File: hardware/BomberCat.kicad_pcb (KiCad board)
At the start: 2 copper layers, 65 x 84.8 mm, 111 parts, among them J1 Battery, J3 MAGSPOOF, J4 MAGSPOOF, P1 USB_C_Plug_USB2.0, Q1 DMG3415U-7, SW1 RESET, SW2 GPIO, SW3 ON, SW4 SOURCE MAG, U1 PN7150B0HN_C11006Y-PN7150B0HN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

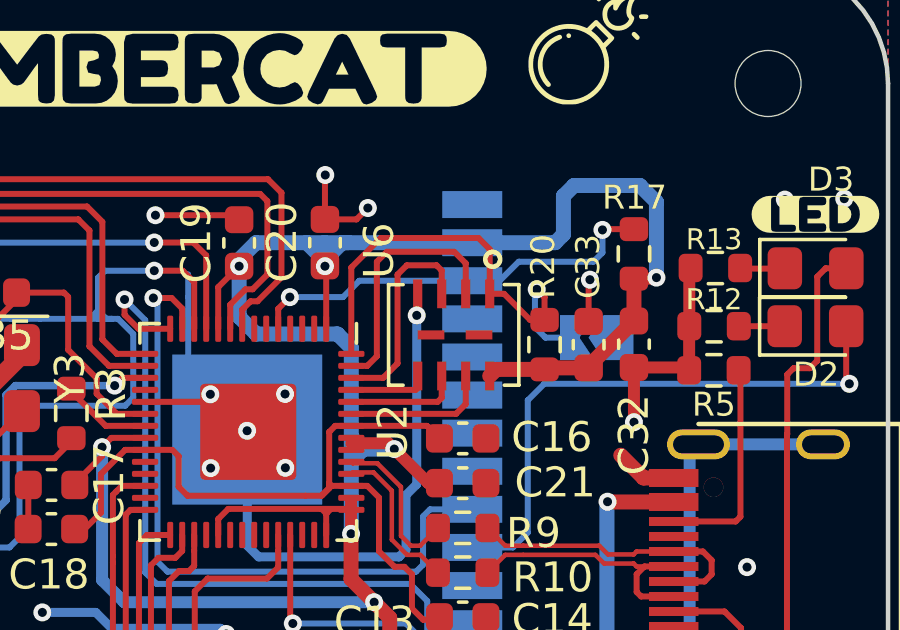
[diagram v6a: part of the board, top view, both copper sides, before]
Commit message: fix(Hw):No_part_Flash_Memory_Changed
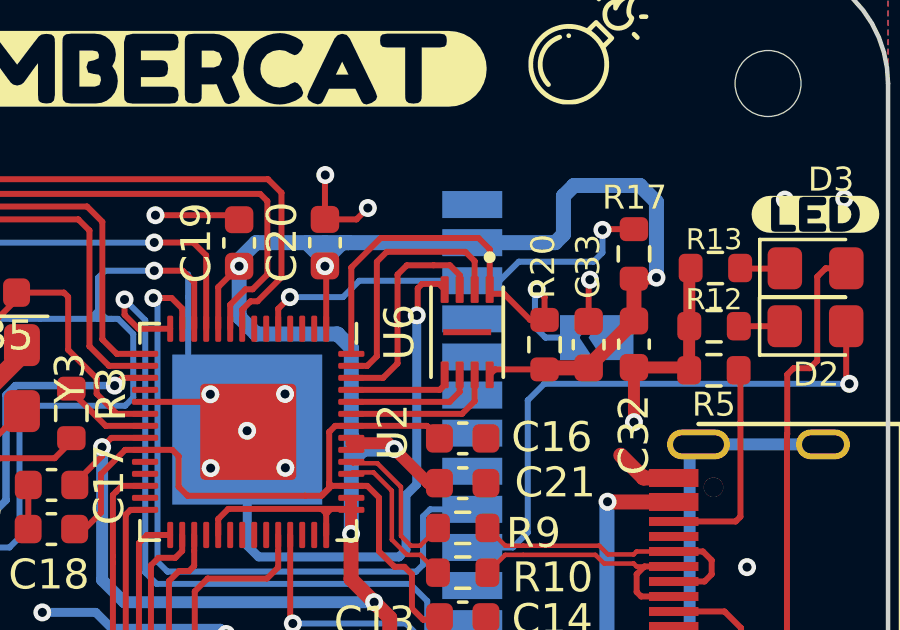
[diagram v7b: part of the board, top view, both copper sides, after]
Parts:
- U6: footprint BomberCat:W25Q16JVUUIQ -> BomberCat:SON50P200X300X40-9N
- moved U6 0.46 mm to (143.0, 148.3)
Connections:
- C35 pad 1: Net-(U2-GPIO14) -> Net-(U2-XIN)
- R3 pad 2: Net-(U2-GPIO16) -> Net-(U2-XOUT)
- U2 pad 10: unconnected-(U2-IOVDD-Pad10) -> +3V3
- U2 pad 11: unconnected-(U2-GPIO8-Pad11) -> /CIPO_TX
- U2 pad 12: unconnected-(U2-GPIO9-Pad12) -> /CS_RX
- U2 pad 13: unconnected-(U2-GPIO10-Pad13) -> /ACK_CTS
- U2 pad 14: unconnected-(U2-GPIO11-Pad14) -> /COPI_RTS
- U2 pad 15: unconnected-(U2-GPIO12-Pad15) -> /SDA
- U2 pad 16: unconnected-(U2-GPIO13-Pad16) -> /SCL
- U2 pad 17: Net-(U2-GPIO14) -> /SCK
- U2 pad 19: unconnected-(U2-TESTEN-Pad19) -> GND
- U2 pad 20: /SCK -> Net-(U2-XIN)
- U2 pad 21: unconnected-(U2-XOUT-Pad21) -> Net-(U2-XOUT)
- U2 pad 23: unconnected-(U2-DVDD-Pad23) -> +1V2
- U2 pad 24: unconnected-(U2-SWCLK-Pad24) -> /SWCLK
- U2 pad 25: unconnected-(U2-SWD-Pad25) -> /SWDIO
- U2 pad 26: unconnected-(U2-RUN-Pad26) -> /RST
- U2 pad 27: Net-(U2-GPIO16) -> unconnected-(U2-GPIO16-Pad27)
- U2 pad 28: unconnected-(U2-GPIO17-Pad28) -> /GPIO1
- U2 pad 29: unconnected-(U2-GPIO18-Pad29) -> /IN_B
- U2 pad 30: unconnected-(U2-GPIO19-Pad30) -> /IN_A
- U2 pad 31: unconnected-(U2-GPIO20-Pad31) -> /ESP_GPIO0
- U2 pad 32: /RST -> unconnected-(U2-GPIO21-Pad32)
- U2 pad 38: unconnected-(U2-GPIO26_ADC0-Pad38) -> /B_ADC
- U2 pad 39: unconnected-(U2-GPIO27_ADC1-Pad39) -> /LED1
- U2 pad 4: /QSPI_DATA0 -> unconnected-(U2-GPIO2-Pad4)
- U2 pad 43: unconnected-(U2-ADC_AVDD-Pad43) -> +3V3
- U2 pad 45: +3V3 -> +1V2
- U2 pad 46: unconnected-(U2-USB_DM-Pad46) -> /RD-
- U2 pad 47: unconnected-(U2-USB_DP-Pad47) -> /RD+
- U2 pad 48: +1V2 -> +3V3
- U2 pad 5: /QSPI_DATA1 -> /ESP_RESET
- U2 pad 50: unconnected-(U2-DVDD-Pad50) -> +1V2
- U2 pad 51: unconnected-(U2-QSPI_SD3-Pad51) -> /QSPI_DATA3
- U2 pad 52: unconnected-(U2-QSPI_SCLK-Pad52) -> /QSPI_SCK
- U2 pad 53: unconnected-(U2-QSPI_SD0-Pad53) -> /QSPI_DATA0
- U2 pad 54: unconnected-(U2-QSPI_SD2-Pad54) -> /QSPI_DATA2
- U2 pad 55: /ESP_RESET -> /QSPI_DATA1
- U2 pad 56: unconnected-(U2-QSPI_SS-Pad56) -> /QSPI_CS
- U2 pad 6: /QSPI_DATA2 -> unconnected-(U2-GPIO4-Pad6)
- U2 pad 7: /QSPI_DATA3 -> unconnected-(U2-GPIO5-Pad7)
- U2 pad 8: unconnected-(U2-GPIO6-Pad8) -> /VEN
- U2 pad 9: unconnected-(U2-GPIO7-Pad9) -> /IRQ
- Y3 pad 1: Net-(U2-GPIO14) -> Net-(U2-XIN)
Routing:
- net Net-(U2-XIN): track 0.00 -> 9.67 mm
- net /SCK: track 19.6 -> 9.97 mm
- net Net-(U2-XOUT): track 0.00 -> 3.03 mm
- net (no net): track 3.03 -> 0.00 mm
- net GND: track 127.9 -> 129.1 mm
- net /QSPI_DATA0: track 2.64 -> 3.52 mm
- net /QSPI_SCK: track 3.80 -> 4.32 mm

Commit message: Feat: fix tag V1.4
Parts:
- removed kibuzzard-67FEA661: G***, kibuzzard-67FEA661
- added kibuzzard-698D0712: G***, kibuzzard-698D0712, B.Cu at (108.3, 145.5)
